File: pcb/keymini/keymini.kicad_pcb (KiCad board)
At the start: 2 copper layers, 205.4 x 88.6 mm, 86 parts, among them J1 USB_C_Receptacle_USB2.0_16P, J2 Conn_01x04, SW1A1 SW_Push, SW1B1 SW_Push, SW1C1 SW_Push, SW1D1 SW_Push, SW1E1 SW_Push, SW1F1 SW_Push, SW1G1 SW_Push, SW1H1 SW_Push, SW1I1 SW_Push, SW1J1 SW_Push, SW2A1 SW_Push, SW2B1 SW_Push, SW2C1 SW_Push, SW2D1 SW_Push, SW2E1 SW_Push, SW2F1 SW_Push, SW2G1 SW_Push, SW2H1 SW_Push, SW2I1 SW_Push, SW2J1 SW_Push, SW3A1 SW_Push, SW3B1 SW_Push, SW3C1 SW_Push, SW3D1 SW_Push, SW3E1 SW_Push, SW3F1 SW_Push, SW3G1 SW_Push, SW3H1 SW_Push, SW3I1 SW_Push, SW3J1 SW_Push, SW4C1 SW_Push, SW4D1 SW_Push, SW4E1 SW_Push, SW4F1 SW_Push, SW4G1 SW_Push, SW4H1 SW_Push, U1 STM32F072CBT6, U2 XC6206P332MR

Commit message: Add copper ground pur on front
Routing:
- net GND: track 152.3 -> 93.1 mm, vias 8 -> 7
- added copper zone on F.Cu, net GND
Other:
- board text added: "Keymini v0.2 by TeXitoi"
- board text removed: "Keymini v0.1 by TeXitoi"
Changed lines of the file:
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@@
 		(sheetname "Racine")
 		(sheetfile "keymini.kicad_sch")
-		(attr smd exclude_from_pos_files exclude_from_bom dnp)
+		(attr smd exclude_from_pos_files)
 		(fp_line
 			(start -1.845 5.2)
@@
 		(sheetname "Racine")
 		(sheetfile "keymini.kicad_sch")
-		(attr smd exclude_from_pos_files exclude_from_bom dnp)
+		(attr smd exclude_from_pos_files)
 		(fp_line
 			(start 3.06 1.85)
@@
 		)
 	)
-	(gr_text "Keymini v0.1 by TeXitoi"
+	(gr_text "Keymini v0.2 by TeXitoi"
 		(at 212 89 21.34)
 		(layer "F.SilkS")
@@
 	)
 	(segment
-		(start 153.25 55.184314)
-		(end 154.4 56.334314)
-		(width 0.2)
-		(layer "F.Cu")
-		(net 2)
-	)
-	(segment
 		(start 145.68 36.805)
 		(end 145.68 36.555)
@@
 	)
 	(segment
-		(start 146.75 37.72)
-		(end 146.75 61.5)
-		(width 0.2)
-		(layer "F.Cu")
-		(net 2)
-	)
-	(segment
 		(start 147 61.75)
 		(end 148 60.75)
@@
 	)
 	(segment
-		(start 153.25 37.72)
-		(end 153.25 55.184314)
-		(width 0.2)
-		(layer "F.Cu")
-		(net 2)
-	)
-	(segment
 		(start 144 87.95)
 		(end 143.05 87)
@@
 	)
 	(segment
-		(start 146.19 104.475)
-		(end 146.19 94.69)
-		(width 0.2)
-		(layer "F.Cu")
-		(net 2)
-	)
-	(segment
 		(start 148 73.05)
 		(end 149.05 72)
@@
 	)
 	(segment
-		(start 146.19 94.69)
-		(end 146 94.5)
-		(width 0.2)
-		(layer "F.Cu")
-		(net 2)
-	)
-	(segment
 		(start 145.68 36.805)
 		(end 145.835 36.805)
@@
 	)
 	(segment
+		(start 153.25 37.72)
+		(end 153.25 42.25)
+		(width 0.2)
+		(layer "F.Cu")
+		(net 2)
+	)
+	(segment
 		(start 149.05 64)
 		(end 149.05 62.8625)
@@
 	)
 	(segment
-		(start 156.95 76.73241)
-		(end 156.95 75)
+		(start 146.75 37.72)
+		(end 146.75 42.25)
 		(width 0.2)
 		(layer "F.Cu")
@@
 	)
 	(segment
-		(start 154.4 63.7875)
-		(end 149.05 69.1375)
+		(start 156.95 76.73241)
+		(end 156.95 75)
 		(width 0.2)
 		(layer "F.Cu")
@@
 	)
 	(segment
-		(start 146.75 61.5)
-		(end 147 61.75)
-		(width 0.2)
-		(layer "F.Cu")
-		(net 2)
-	)
-	(segment
 		(start 150.75 85.1625)
 		(end 150.75 85.998096)
@@
 	)
 	(segment
-		(start 154.4 56.334314)
-		(end 154.4 63.7875)
-		(width 0.2)
-		(layer "F.Cu")
-		(net 2)
-	)
-	(segment
 		(start 150.75 85.998096)
 		(end 151.751904 87)
@@
 	)
 	(via
-		(at 146 94.5)
-		(size 0.6)
-		(drill 0.3)
-		(layers "F.Cu" "B.Cu")
-		(free yes)
-		(net 2)
-	)
-	(via
 		(at 144 88.5)
 		(size 0.6)
@@
 	)
 	(zone
+		(net 0)
+		(net_name "")
+		(layer "F.Cu")
+		(hatch edge 0.5)
+		(connect_pads
+			(clearance 0)
+		)
+		(min_thickness 0.25)
+		(filled_areas_thickness no)
+		(keepout
+			(tracks allowed)
+			(vias allowed)
+			(pads allowed)
+			(copperpour not_allowed)
+			(footprints allowed)
+		)
+		(fill
+			(thermal_gap 0.5)
+			(thermal_bridge_width 0.5)
+		)
+		(polygon
+			(pts
+				(xy 150 40) (xy 137 89) (xy 150 93) (xy 163 89)
+			)
+		)
+	)
+	(zone
 		(net 2)
 		(net_name "GND")
-		(layer "B.Cu")
+		(layers "F&B.Cu")
 		(hatch edge 0.5)
 		(connect_pads
@@
 		(polygon
 			(pts
-				(xy 157 16) (xy 260 16) (xy 260 124) (xy 38 124) (xy 38 16) (xy 143 16) (xy 143 41) (xy 157 41)
+				(xy 156 16) (xy 260 16) (xy 260 124) (xy 38 124) (xy 38 16) (xy 144 16) (xy 144 40) (xy 156 40)
 			)
 		)

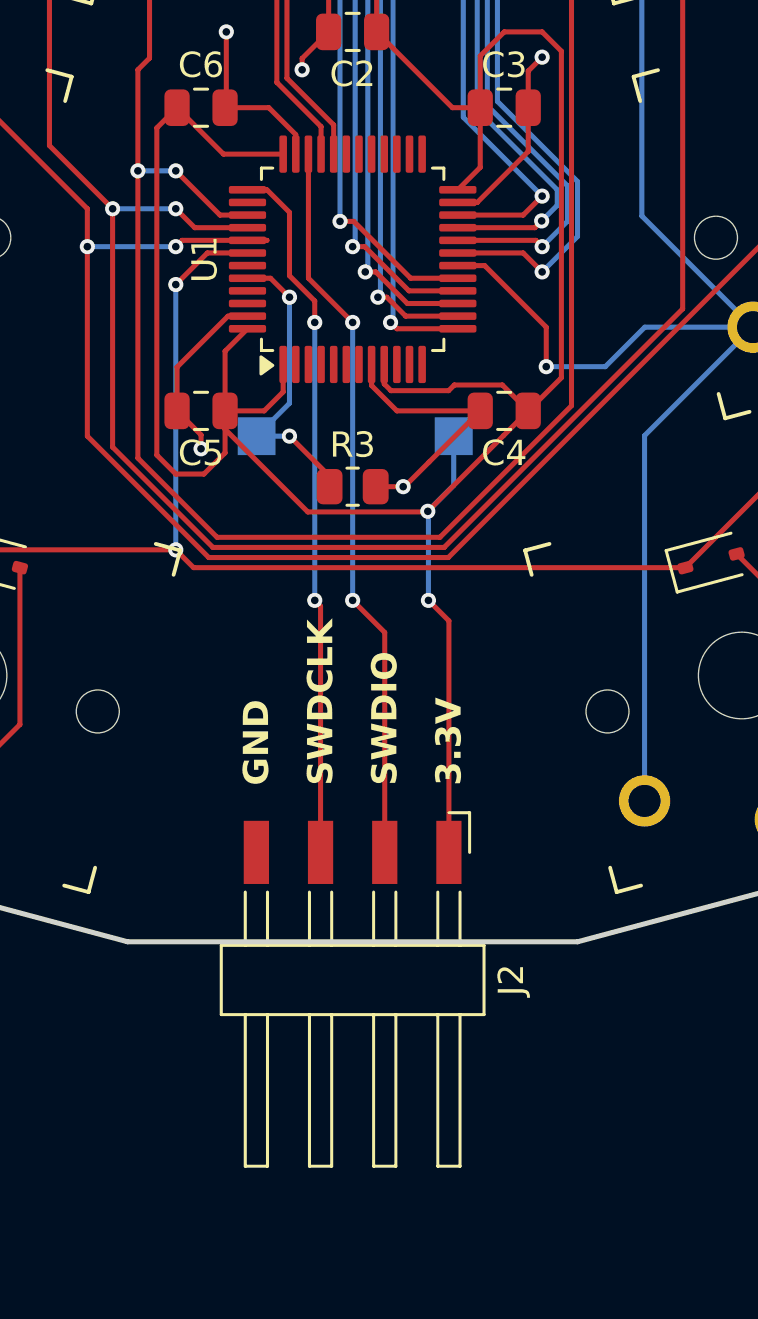
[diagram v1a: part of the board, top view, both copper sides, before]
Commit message: Remove SWD connector
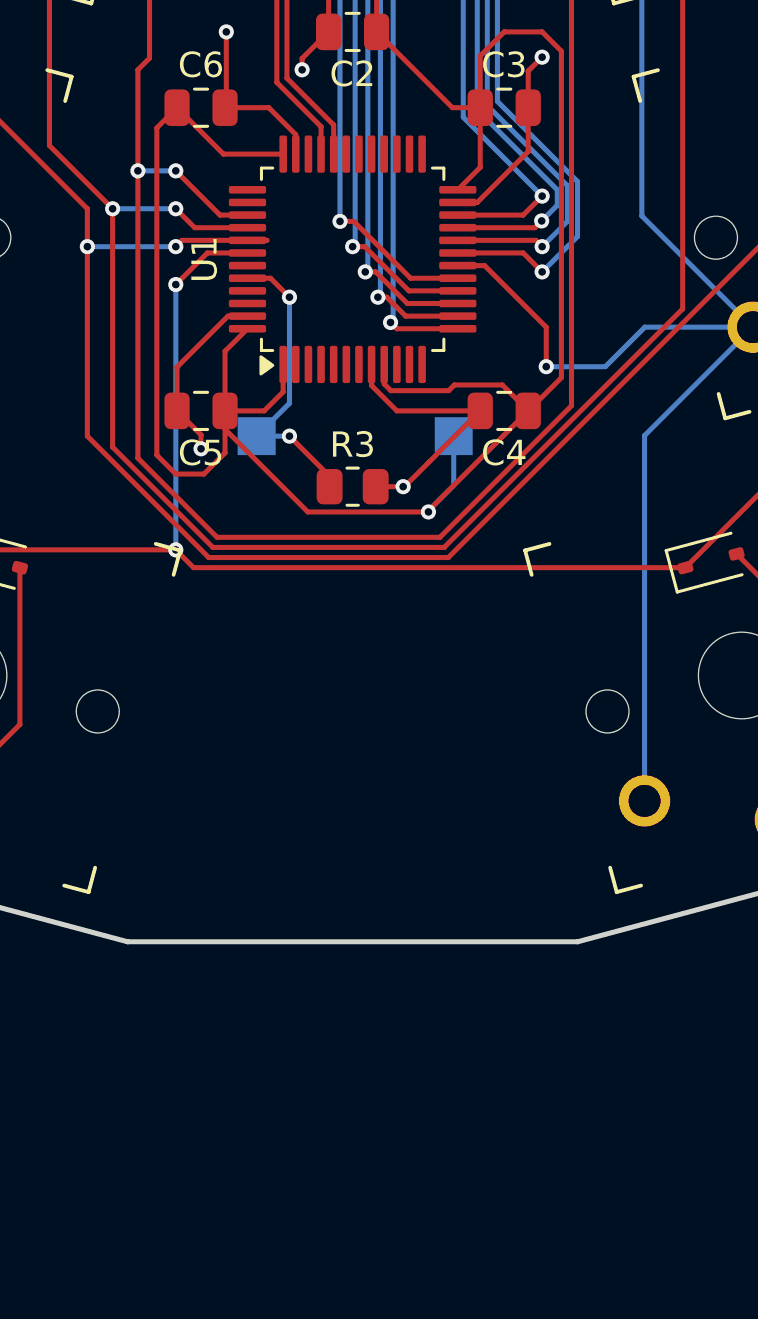
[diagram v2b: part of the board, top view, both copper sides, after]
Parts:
- removed J2: Conn_01x04, Connector_Harwin:Harwin_M20-89004xx_1x04_P2.54mm_Horizontal
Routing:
- net SWDIO: track 28.9 -> 0.00 mm, vias 2 -> 0
- net SWDCLK: track 27.9 -> 0.00 mm, vias 2 -> 0
- net +3.3V: track 104.0 -> 90.2 mm, vias 2 -> 1
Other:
- board text removed: "3.3V"
- board text removed: "GND"
- board text removed: "SWDCLK"
- board text removed: "SWDIO"

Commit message: v0.2 gerber
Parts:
- renumbered BOOT1 to BOOT0
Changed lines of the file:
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@@
 			(drillshape 0)
 			(scaleselection 1)
-			(outputdirectory "../gerbers/v0.1/keymini/")
+			(outputdirectory "../gerbers/v0.2/keymini/")
 		)
 	)
@@
 		(descr "https://www.mouser.com/ds/2/60/RS-282G05A-SM_RT-1159762.pdf")
 		(tags "SPST button tactile switch")
-		(property "Reference" "BOOT1"
+		(property "Reference" "BOOT0"
 			(at 0 2.6 0)
 			(layer "B.SilkS")
